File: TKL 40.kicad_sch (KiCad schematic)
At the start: 122 parts, among them SW1 SW_Push, SW10 SW_Push, SW11 SW_Push, SW12 SW_Push, SW13 SW_Push, SW14 SW_Push, SW15 SW_Push, SW16 SW_Push, SW17 SW_Push, SW18 SW_Push, SW19 SW_Push, SW2 SW_Push, SW20 SW_Push, SW21 SW_Push, SW22 SW_Push, SW23 SW_Push, SW24 SW_Push, SW24_1 SW_Push, SW25 SW_Push, SW26 SW_Push, SW27 SW_Push, SW28 SW_Push, SW29 SW_Push, SW3 SW_Push, SW30 SW_Push, SW31 SW_Push, SW32 SW_Push, SW33 SW_Push, SW34 SW_Push, SW35 SW_Push, SW35_1 SW_Push, SW35_2 SW_Push, SW36 SW_Push, SW36_1 SW_Push, SW37 SW_Push, SW38 SW_Push, SW39 SW_Push, SW4 SW_Push, SW40 SW_Push, SW41 SW_Push, SW42 SW_Push, SW43 SW_Push, SW44 SW_Push, SW45 SW_Push, SW46 SW_Push, SW47 SW_Push, SW47_1 SW_Push, SW48 SW_Push, SW48_1 SW_Push, SW49 SW_Push, SW5 SW_Push, SW50 SW_Push, SW51 SW_Push, SW52 SW_Push, SW53 SW_Push, SW54 SW_Push, SW55 SW_Push, SW56 SW_Push, SW56_1 SW_Push, SW57 SW_Push, SW57_1 SW_Push, SW6 SW_Push, SW7 SW_Push, SW8 SW_Push, SW9 SW_Push

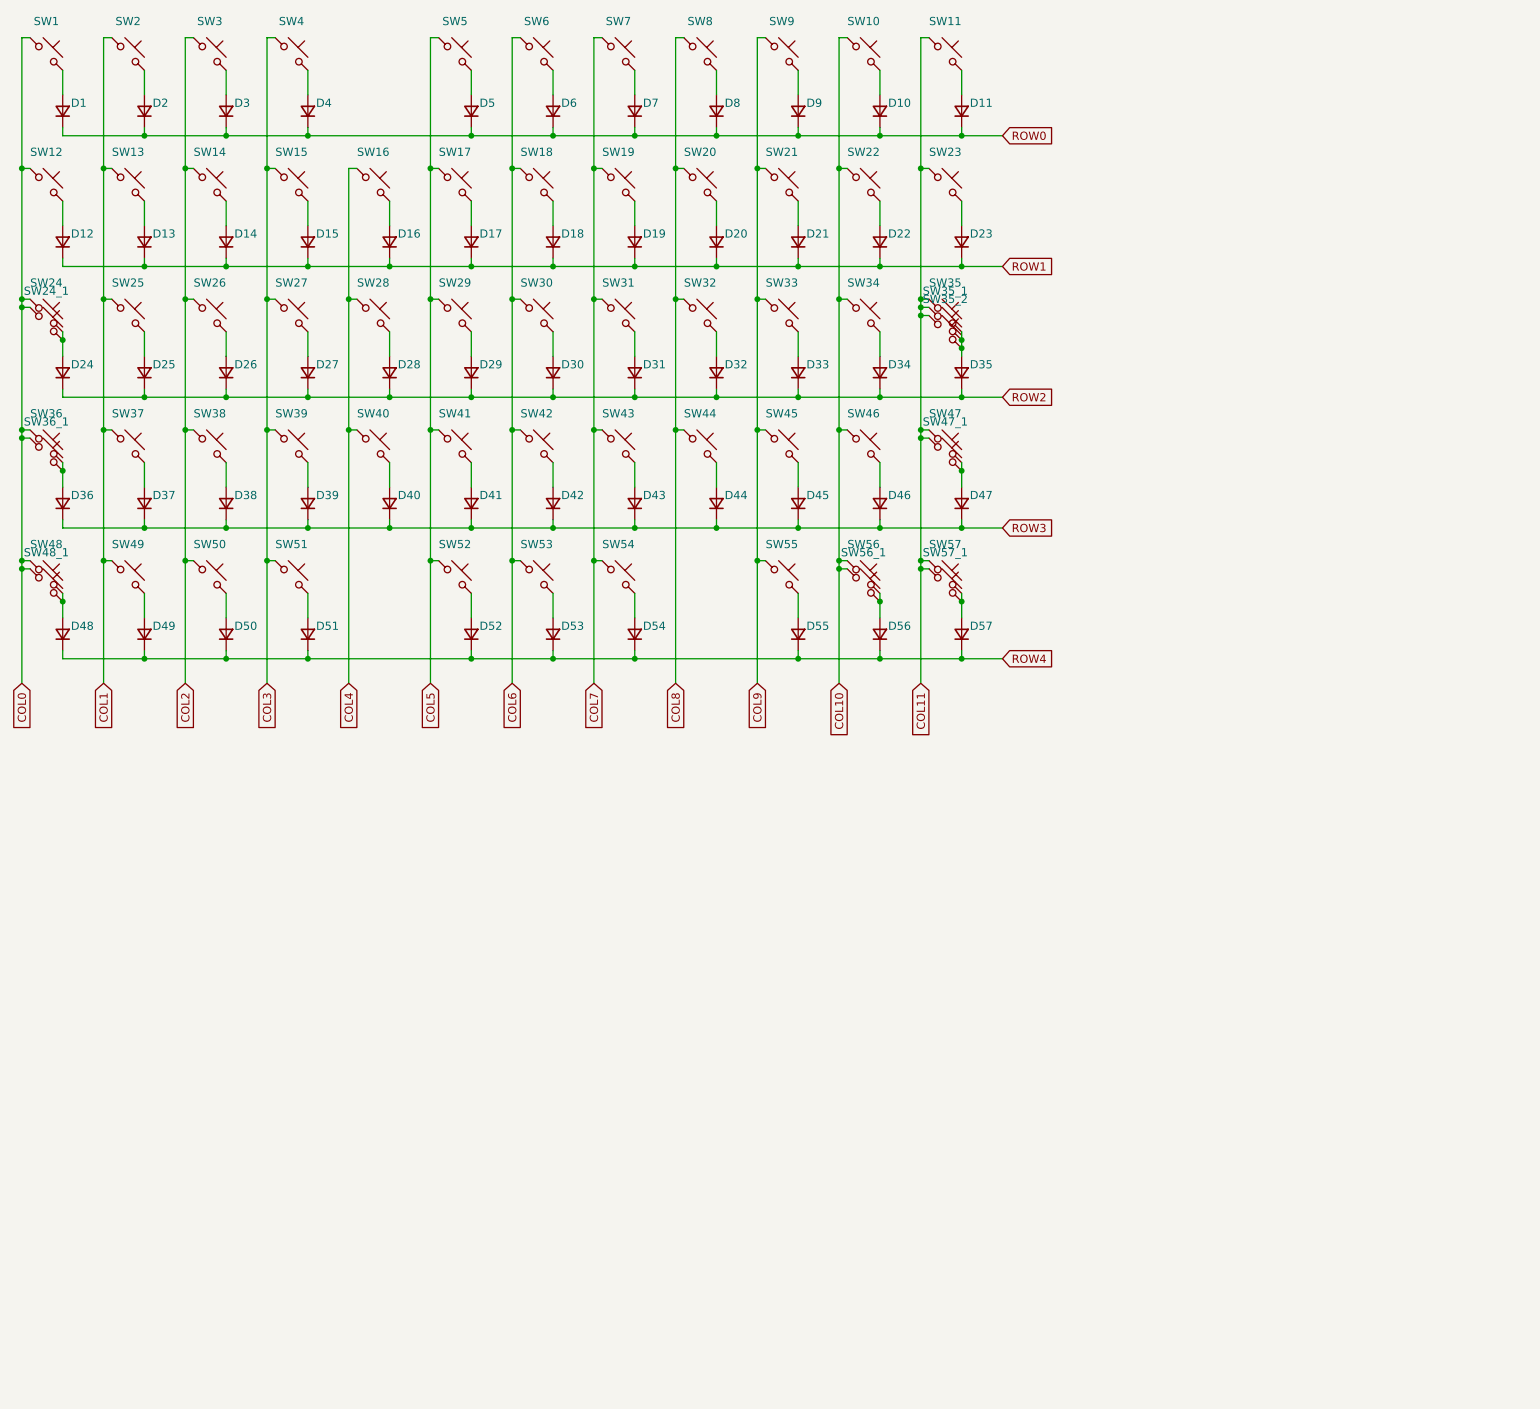
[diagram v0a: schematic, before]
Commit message: Added MCU, ESD, and some routing
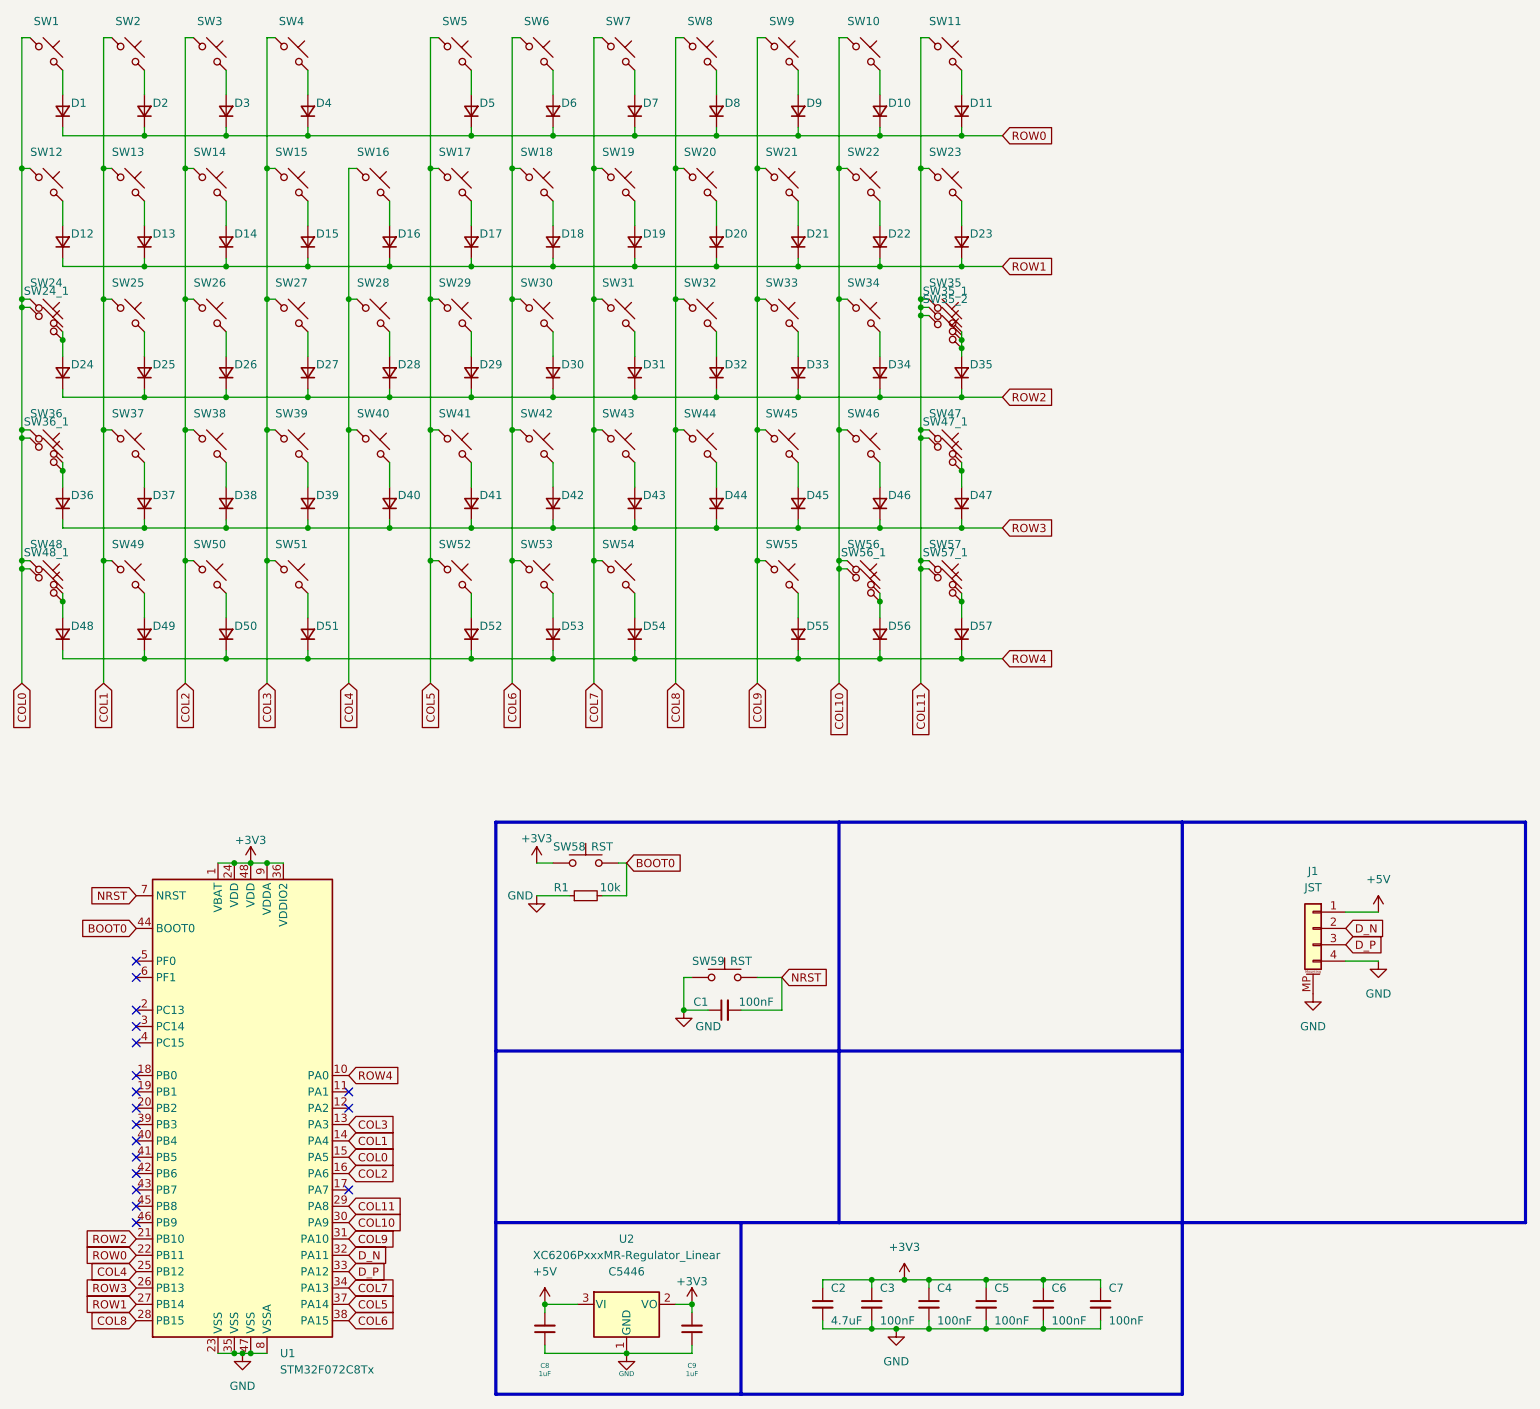
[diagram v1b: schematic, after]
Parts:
- added C1, C3, C4, C5, C6, C7: 100nF, Capacitor_SMD:C_0402_1005Metric, symbol Device:C_Small
- added C2: 4.7uF, Capacitor_SMD:C_0402_1005Metric, symbol Device:C_Small
- added C8, C9: 1uF, Capacitor_SMD:C_0402_1005Metric, symbol Device:C_Small
- added J1: JST, acheron_Connectors.pretty-master:MOLEX_781710004_MountingReliefs, symbol Connector_Generic_MountingPin:Conn_01x04_MountingPin
- added R1: 10k, Resistor_SMD:R_0402_1005Metric, symbol Device:R_Small
- added SW58, SW59: RST, Button_Switch_SMD:SW_SPST_SKQG_WithoutStem, symbol Switch:SW_Push
- added U1: STM32F072C8Tx, Package_QFP:LQFP-48_7x7mm_P0.5mm, symbol MCU_ST_STM32F0:STM32F072C8Tx
- added U2: XC6206PxxxMR-Regulator_Linear, Package_TO_SOT_SMD:SOT-23, symbol kicad-keyboard-parts:XC6206PxxxMR-Regulator_Linear
- SW1, SW10, SW11, SW13, SW14, SW15, SW16, SW17, SW18, SW19, SW2, SW20, SW21, SW22, SW25, SW26, SW27, SW28, SW29, SW3, SW30, SW31, SW32, SW33, SW34, SW37, SW38, SW39, SW4, SW40, SW41, SW42, SW43, SW44, SW45, SW46, SW5, SW50, SW51, SW55, SW56_1, SW6, SW7, SW8, SW9: footprint Switch_Keyboard_Hotswap_Kailh:SW_Hotswap_Kailh_MX_1.00u -> Switch_Keyboard_Hotswap_Kailh:SW_Hotswap_Kailh_MX_Plated_1.00u
- SW12, SW23, SW48, SW49, SW56, SW57: footprint Switch_Keyboard_Hotswap_Kailh:SW_Hotswap_Kailh_MX_1.50u -> Switch_Keyboard_Hotswap_Kailh:SW_Hotswap_Kailh_MX_Plated_1.50u
- SW24: footprint Switch_Keyboard_Hotswap_Kailh:SW_Hotswap_Kailh_MX_1.75u_90deg -> Switch_Keyboard_Hotswap_Kailh:SW_Hotswap_Kailh_MX_Plated_1.75u_90deg
- SW24_1: footprint Switch_Keyboard_Hotswap_Kailh:SW_Hotswap_Kailh_MX_1.25u_90deg -> Switch_Keyboard_Hotswap_Kailh:SW_Hotswap_Kailh_MX_Plated_1.25u_90deg
- SW35, SW36, SW48_1, SW57_1: footprint Switch_Keyboard_Hotswap_Kailh:SW_Hotswap_Kailh_MX_1.25u -> Switch_Keyboard_Hotswap_Kailh:SW_Hotswap_Kailh_MX_Plated_1.25u
- SW35_1: footprint Switch_Keyboard_Hotswap_Kailh:SW_Hotswap_Kailh_MX_ISOEnter_270deg -> Switch_Keyboard_Hotswap_Kailh:SW_Hotswap_Kailh_MX_Plated_ISOEnter_270deg
- SW35_2: footprint Switch_Keyboard_Hotswap_Kailh:SW_Hotswap_Kailh_MX_2.25u_90deg -> Switch_Keyboard_Hotswap_Kailh:SW_Hotswap_Kailh_MX_Plated_2.25u
- SW36_1, SW54: footprint Switch_Keyboard_Hotswap_Kailh:SW_Hotswap_Kailh_MX_2.25u -> Switch_Keyboard_Hotswap_Kailh:SW_Hotswap_Kailh_MX_Plated_2.25u
- SW47: footprint Switch_Keyboard_Hotswap_Kailh:SW_Hotswap_Kailh_MX_1.75u -> Switch_Keyboard_Hotswap_Kailh:SW_Hotswap_Kailh_MX_Plated_1.75u
- SW47_1, SW52: footprint Switch_Keyboard_Hotswap_Kailh:SW_Hotswap_Kailh_MX_2.75u -> Switch_Keyboard_Hotswap_Kailh:SW_Hotswap_Kailh_MX_Plated_2.75u
- SW53: footprint Switch_Keyboard_Hotswap_Kailh:SW_Hotswap_Kailh_MX_7.00u -> Switch_Keyboard_Hotswap_Kailh:SW_Hotswap_Kailh_MX_Plated_7.00u
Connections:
- net COL0: now also U1.15 (PA5)
- net COL1: now also U1.14 (PA4)
- net COL10: now also U1.30 (PA9)
- net COL11: now also U1.29 (PA8)
- net COL2: now also U1.16 (PA6)
- net COL3: now also U1.13 (PA3)
- net COL4: now also U1.25 (PB12)
- net COL5: now also U1.37 (PA14)
- net COL6: now also U1.38 (PA15)
- net COL7: now also U1.34 (PA13)
- net COL8: now also U1.28 (PB15)
- net COL9: now also U1.31 (PA10)
- net ROW0: now also U1.22 (PB11)
- net ROW1: now also U1.27 (PB14)
- net ROW2: now also U1.21 (PB10)
- net ROW3: now also U1.26 (PB13)
- net ROW4: now also U1.10 (PA0)
- new net +3V3: C2.1, C3.1, C4.1, C5.1, C6.1, C7.1, C9.2, SW58.1, U1.1 (VBAT), U1.24 (VDD), U1.36 (VDDIO2), U1.48 (VDD), U1.9 (VDDA), U2.2 (VO)
- new net +5V: C8.2, J1.1 (Pin_1), U2.3 (VI)
- new net BOOT0: R1.2, SW58.2, U1.44 (BOOT0)
- new net D_N: J1.2 (Pin_2), U1.32 (PA11)
- new net D_P: J1.3 (Pin_3), U1.33 (PA12)
- new net GND: C1.1, C2.2, C3.2, C4.2, C5.2, C6.2, C7.2, C8.1, C9.1, J1.4 (Pin_4), J1.MP (MountPin), R1.1, SW59.1, U1.23 (VSS), U1.35 (VSS), U1.47 (VSS), U1.8 (VSSA), U2.1 (GND)
- new net NRST: C1.2, SW59.2, U1.7 (NRST)
- no-connect marks 0 -> 18
